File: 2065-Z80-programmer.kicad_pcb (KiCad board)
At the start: 2 copper layers, 100 x 65 mm, 29 parts, among them J1 Conn_01x05, J2 Conn_02x20_Counter_Clockwise, J3 Conn_01x02, J4 Conn_02x20_Odd_Even, Q1 2N7000, Q2 2N7000, Q3 PN2222, U1 MCP23017-E_SP, U2 MCP23017-E_SP

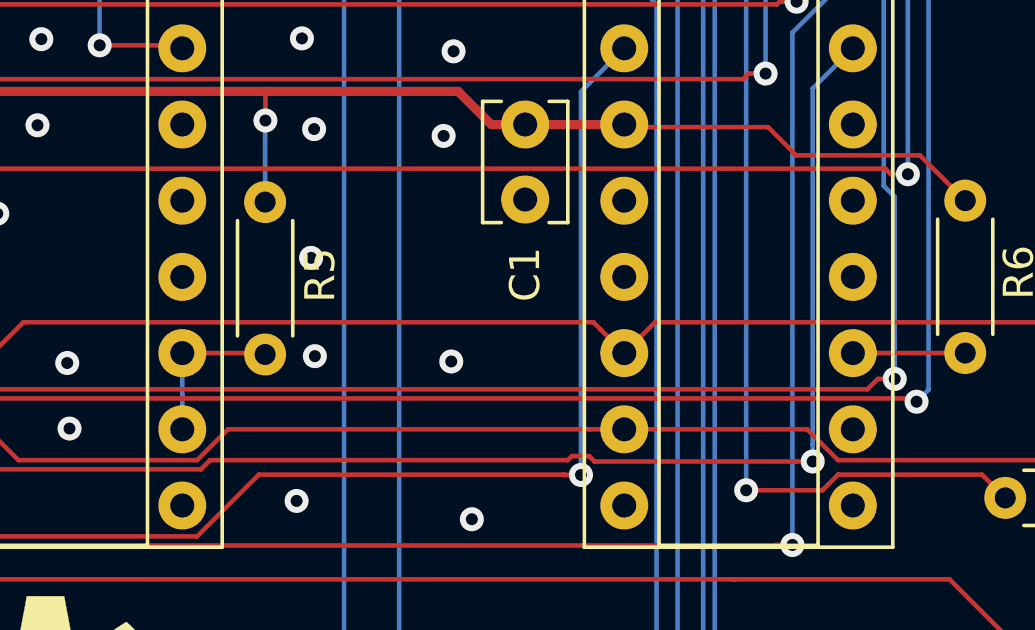
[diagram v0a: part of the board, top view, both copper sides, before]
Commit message: Pull up /RESET
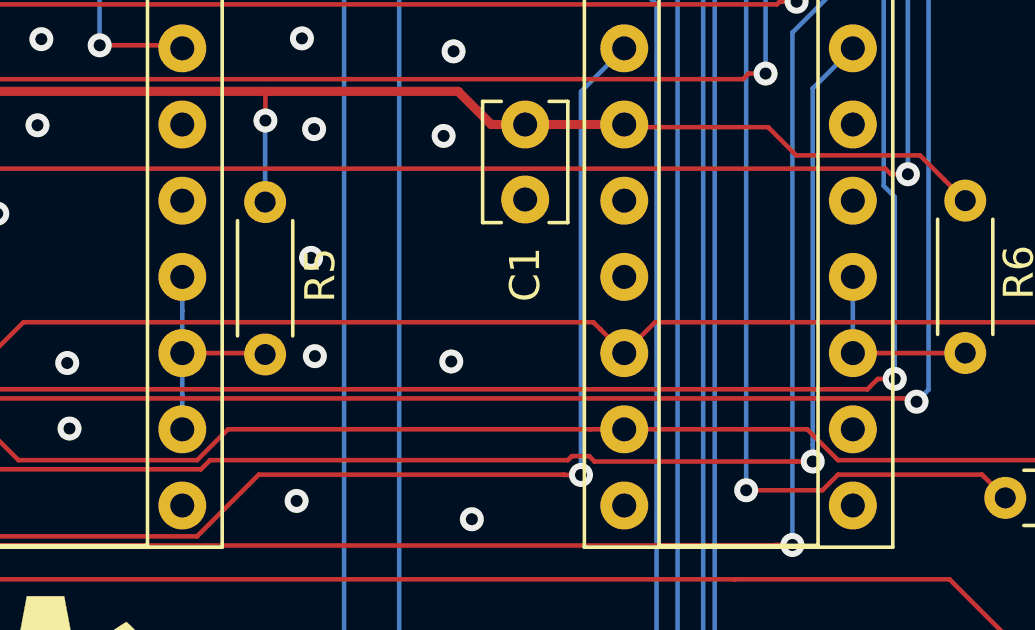
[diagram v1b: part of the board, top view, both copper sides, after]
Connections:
- U1 pad 18: Net-(U1-Pad18) -> Net-(R5-Pad1)
- U2 pad 18: Net-(U2-Pad18) -> Net-(R6-Pad1)
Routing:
- net Net-(R5-Pad1): track 5.32 -> 7.86 mm
- net Net-(R6-Pad1): track 3.75 -> 6.29 mm

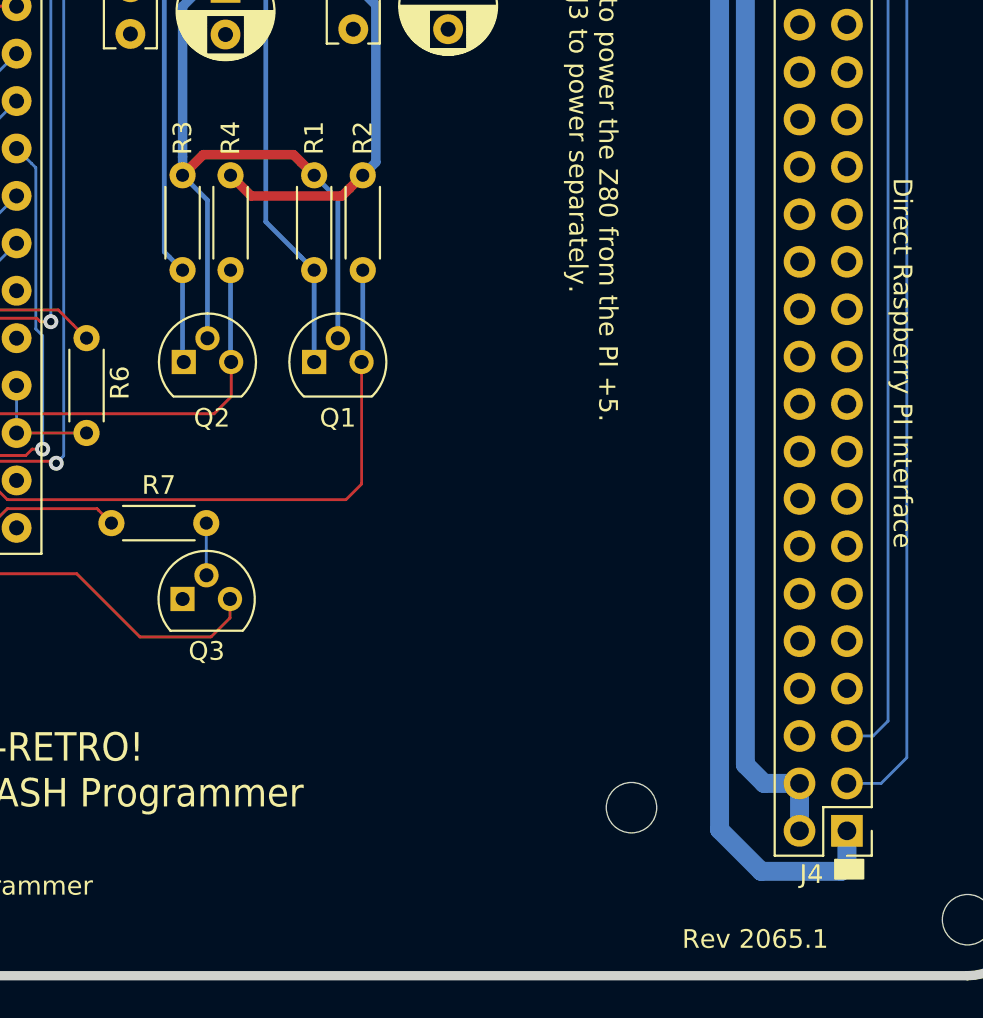
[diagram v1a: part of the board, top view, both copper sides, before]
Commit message: Add 5V clamping diodes to I2C lines Move mounting hole clear of user-1 header
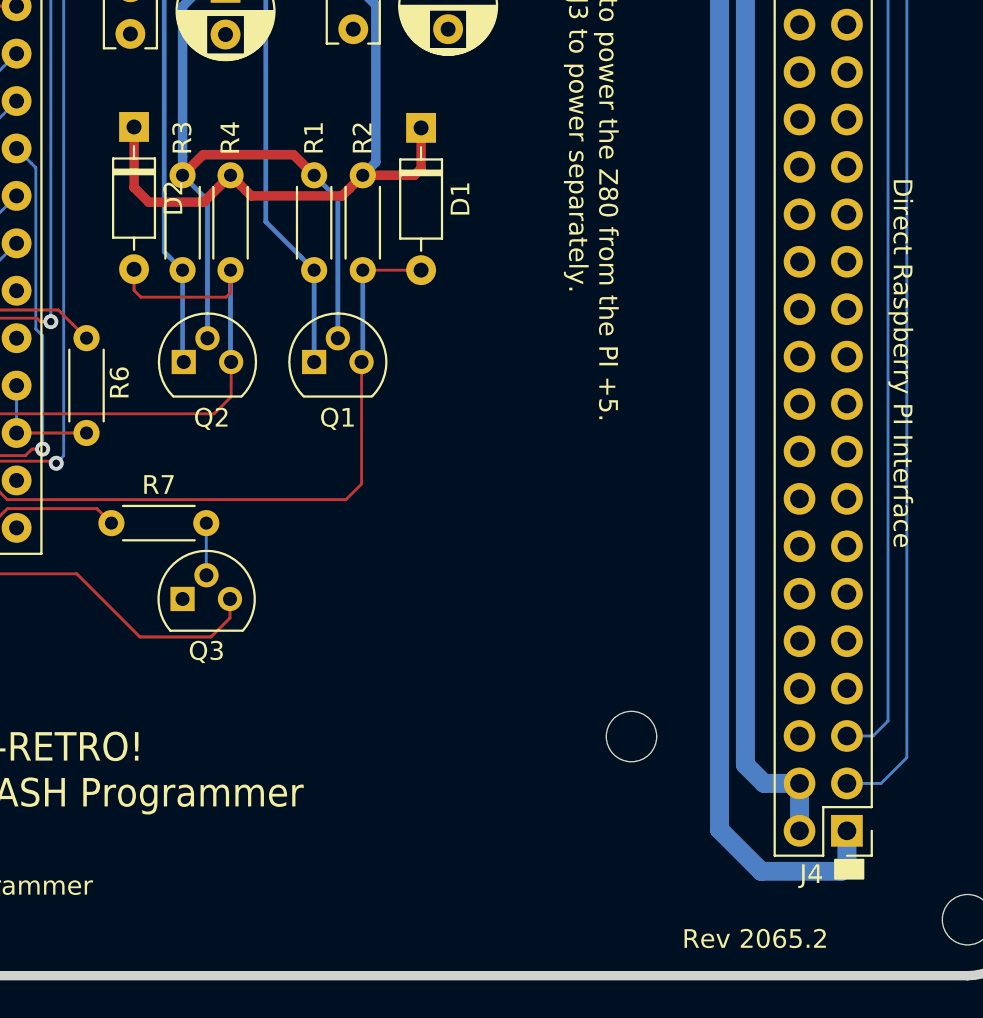
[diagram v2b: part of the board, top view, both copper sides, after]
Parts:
- added D1: 1N914, Diode_THT:D_DO-35_SOD27_P7.62mm_Horizontal, F.Cu at (152.7, 74.6)
- added D2: 1N914, Diode_THT:D_DO-35_SOD27_P7.62mm_Horizontal, F.Cu at (137.4, 74.5)
- moved H5 3.81 mm to (164.0, 107.2)
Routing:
- net +5V: track 179.0 -> 193.7 mm
- net /SCK: track 49.9 -> 57.7 mm
- net /SDA: track 61.6 -> 64.7 mm
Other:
- board text added: "Rev 2065.2"
- board text removed: "Rev 2065.1"
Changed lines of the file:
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@@
     (thickness 1.6)
     (drawings 29)
-    (tracks 476)
+    (tracks 490)
     (zones 0)
-    (modules 29)
+    (modules 31)
     (nets 86)
   )
   (page A4)
+  (title_block
+    (date 2021-10-18)
+    (rev 2.0)
+  )
   (layers
     (0 F.Cu signal)
@@
     (add_net "Net-(U2-Pad20)")
   )
+  (module Diode_THT:D_DO-35_SOD27_P7.62mm_Horizontal (layer F.Cu)
+    (at 137.35558 74.53884 270)
+    (descr "Diode, DO-35_SOD27 series, Axial, Horizontal, pin pitch=7.62mm, , length*diameter=4*2mm^2, , http://www.diodes.com/_files/packages/DO-35.pdf")
+    (tags "Diode DO-35_SOD27 series Axial Horizontal pin pitch 7.62mm  length 4mm diameter 2mm")
+    (fp_text reference D2 (at 3.81 -2.12 90) (layer F.SilkS)
+      (effects (font (size 1 1) (thickness 0.15)))
+    )
+    (fp_text value 1N914 (at 3.81 2.12 90) (layer F.Fab)
+      (effects (font (size 1 1) (thickness 0.15)))
+    )
+    (fp_text user K (at 0 -1.8 90) (layer F.SilkS) hide
+      (effects (font (size 1 1) (thickness 0.15)))
+    )
+    (fp_text user K (at 0 -1.8 90) (layer F.Fab)
+      (effects (font (size 1 1) (thickness 0.15)))
+    )
+    (fp_text user %R (at 4.11 0 90) (layer F.Fab)
+      (effects (font (size 0.8 0.8) (thickness 0.12)))
+    )
+    (fp_line (start 8.67 -1.25) (end -1.05 -1.25) (layer F.CrtYd) (width 0.05))
+    (fp_line (start 8.67 1.25) (end 8.67 -1.25) (layer F.CrtYd) (width 0.05))
+    (fp_line (start -1.05 1.25) (end 8.67 1.25) (layer F.CrtYd) (width 0.05))
+    (fp_line (start -1.05 -1.25) (end -1.05 1.25) (layer F.CrtYd) (width 0.05))
+    (fp_line (start 2.29 -1.12) (end 2.29 1.12) (layer F.SilkS) (width 0.12))
+    (fp_line (start 2.53 -1.12) (end 2.53 1.12) (layer F.SilkS) (width 0.12))
+    (fp_line (start 2.41 -1.12) (end 2.41 1.12) (layer F.SilkS) (width 0.12))
+    (fp_line (start 6.58 0) (end 5.93 0) (layer F.SilkS) (width 0.12))
+    (fp_line (start 1.04 0) (end 1.69 0) (layer F.SilkS) (width 0.12))
+    (fp_line (start 5.93 -1.12) (end 1.69 -1.12) (layer F.SilkS) (width 0.12))
+    (fp_line (start 5.93 1.12) (end 5.93 -1.12) (layer F.SilkS) (width 0.12))
+    (fp_line (start 1.69 1.12) (end 5.93 1.12) (layer F.SilkS) (width 0.12))
+    (fp_line (start 1.69 -1.12) (end 1.69 1.12) (layer F.SilkS) (width 0.12))
+    (fp_line (start 2.31 -1) (end 2.31 1) (layer F.Fab) (width 0.1))
+    (fp_line (start 2.51 -1) (end 2.51 1) (layer F.Fab) (width 0.1))
+    (fp_line (start 2.41 -1) (end 2.41 1) (layer F.Fab) (width 0.1))
+    (fp_line (start 7.62 0) (end 5.81 0) (layer F.Fab) (width 0.1))
+    (fp_line (start 0 0) (end 1.81 0) (layer F.Fab) (width 0.1))
+    (fp_line (start 5.81 -1) (end 1.81 -1) (layer F.Fab) (width 0.1))
+    (fp_line (start 5.81 1) (end 5.81 -1) (layer F.Fab) (width 0.1))
+    (fp_line (start 1.81 1) (end 5.81 1) (layer F.Fab) (width 0.1))
+    (fp_line (start 1.81 -1) (end 1.81 1) (layer F.Fab) (width 0.1))
+    (pad 2 thru_hole oval (at 7.62 0 270) (size 1.6 1.6) (drill 0.8) (layers *.Cu *.Mask)
+      (net 13 /SCK))
+    (pad 1 thru_hole rect (at 0 0 270) (size 1.6 1.6) (drill 0.8) (layers *.Cu *.Mask)
+      (net 12 +5V))
+    (model ${KISYS3DMOD}/Diode_THT.3dshapes/D_DO-35_SOD27_P7.62mm_Horizontal.wrl
+      (at (xyz 0 0 0))
+      (scale (xyz 1 1 1))
+      (rotate (xyz 0 0 0))
+    )
+  )
+  (module Diode_THT:D_DO-35_SOD27_P7.62mm_Horizontal (layer F.Cu)
+    (at 152.7302 74.58964 270)
+    (descr "Diode, DO-35_SOD27 series, Axial, Horizontal, pin pitch=7.62mm, , length*diameter=4*2mm^2, , http://www.diodes.com/_files/packages/DO-35.pdf")
+    (tags "Diode DO-35_SOD27 series Axial Horizontal pin pitch 7.62mm  length 4mm diameter 2mm")
+    (fp_text reference D1 (at 3.81 -2.12 90) (layer F.SilkS)
+      (effects (font (size 1 1) (thickness 0.15)))
+    )
+    (fp_text value 1N914 (at 3.81 2.12 90) (layer F.Fab)
+      (effects (font (size 1 1) (thickness 0.15)))
+    )
+    (fp_text user K (at 0 -1.8 90) (layer F.SilkS) hide
+      (effects (font (size 1 1) (thickness 0.15)))
+    )
+    (fp_text user K (at 0 -1.8 90) (layer F.Fab)
+      (effects (font (size 1 1) (thickness 0.15)))
+    )
+    (fp_text user %R (at 4.11 0 90) (layer F.Fab)
+      (effects (font (size 0.8 0.8) (thickness 0.12)))
+    )
+    (fp_line (start 8.67 -1.25) (end -1.05 -1.25) (layer F.CrtYd) (width 0.05))
+    (fp_line (start 8.67 1.25) (end 8.67 -1.25) (layer F.CrtYd) (width 0.05))
+    (fp_line (start -1.05 1.25) (end 8.67 1.25) (layer F.CrtYd) (width 0.05))
+    (fp_line (start -1.05 -1.25) (end -1.05 1.25) (layer F.CrtYd) (width 0.05))
+    (fp_line (start 2.29 -1.12) (end 2.29 1.12) (layer F.SilkS) (width 0.12))
+    (fp_line (start 2.53 -1.12) (end 2.53 1.12) (layer F.SilkS) (width 0.12))
+    (fp_line (start 2.41 -1.12) (end 2.41 1.12) (layer F.SilkS) (width 0.12))
+    (fp_line (start 6.58 0) (end 5.93 0) (layer F.SilkS) (width 0.12))
+    (fp_line (start 1.04 0) (end 1.69 0) (layer F.SilkS) (width 0.12))
+    (fp_line (start 5.93 -1.12) (end 1.69 -1.12) (layer F.SilkS) (width 0.12))
+    (fp_line (start 5.93 1.12) (end 5.93 -1.12) (layer F.SilkS) (width 0.12))
+    (fp_line (start 1.69 1.12) (end 5.93 1.12) (layer F.SilkS) (width 0.12))
+    (fp_line (start 1.69 -1.12) (end 1.69 1.12) (layer F.SilkS) (width 0.12))
+    (fp_line (start 2.31 -1) (end 2.31 1) (layer F.Fab) (width 0.1))
+    (fp_line (start 2.51 -1) (end 2.51 1) (layer F.Fab) (width 0.1))
+    (fp_line (start 2.41 -1) (end 2.41 1) (layer F.Fab) (width 0.1))
+    (fp_line (start 7.62 0) (end 5.81 0) (layer F.Fab) (width 0.1))
+    (fp_line (start 0 0) (end 1.81 0) (layer F.Fab) (width 0.1))
+    (fp_line (start 5.81 -1) (end 1.81 -1) (layer F.Fab) (width 0.1))
+    (fp_line (start 5.81 1) (end 5.81 -1) (layer F.Fab) (width 0.1))
+    (fp_line (start 1.81 1) (end 5.81 1) (layer F.Fab) (width 0.1))
+    (fp_line (start 1.81 -1) (end 1.81 1) (layer F.Fab) (width 0.1))
+    (pad 2 thru_hole oval (at 7.62 0 270) (size 1.6 1.6) (drill 0.8) (layers *.Cu *.Mask)
+      (net 11 /SDA))
+    (pad 1 thru_hole rect (at 0 0 270) (size 1.6 1.6) (drill 0.8) (layers *.Cu *.Mask)
+      (net 12 +5V))
+    (model ${KISYS3DMOD}/Diode_THT.3dshapes/D_DO-35_SOD27_P7.62mm_Horizontal.wrl
+      (at (xyz 0 0 0))
+      (scale (xyz 1 1 1))
+      (rotate (xyz 0 0 0))
+    )
+  )
   (module MountingHole:MountingHole_2.7mm_M2.5_DIN965 (layer F.Cu)
-    (at 164 111)
+    (at 164 107.19)
     (descr "Mounting Hole 2.7mm, no annular, M2.5, DIN965")
     (tags "mounting hole 2.7mm no annular m2.5 din965")
@@
     )
   )
-  (gr_text "Rev 2065.1" (at 166.70528 118.04396) (layer F.SilkS)
+  (gr_text "Rev 2065.2" (at 166.70528 118.04396) (layer F.SilkS)
     (effects (font (size 1 1) (thickness 0.15)) (justify left))
   )
@@
   (segment (start 149.542 93.663) (end 149.542 87.128) (width 0.1524) (layer F.Cu) (net 11))
   (segment (start 148.704399 94.500601) (end 149.542 93.663) (width 0.1524) (layer F.Cu) (net 11))
+  (segment (start 152.72856 82.208) (end 152.7302 82.20964) (width 0.1524) (layer F.Cu) (net 11))
+  (segment (start 149.606 82.208) (end 152.72856 82.208) (width 0.1524) (layer F.Cu) (net 11))
   (segment (start 155.512 58.166) (end 148.082 58.166) (width 1.016) (layer B.Cu) (net 12))
   (segment (start 148.082 65.786) (end 149.098 66.802) (width 0.508) (layer B.Cu) (net 12))
@@
   (segment (start 96.65863 83.312) (end 96.00202 83.96861) (width 0.3048) (layer F.Cu) (net 12))
   (segment (start 92.46842 83.96861) (end 91.75 83.96861) (width 0.3048) (layer F.Cu) (net 12))
+  (segment (start 149.606 77.128) (end 152.361 77.128) (width 0.508) (layer F.Cu) (net 12))
+  (segment (start 152.7302 76.7588) (end 152.7302 74.58964) (width 0.508) (layer F.Cu) (net 12))
+  (segment (start 152.361 77.128) (end 152.7302 76.7588) (width 0.508) (layer F.Cu) (net 12))
+  (segment (start 142.524 77.128) (end 141.08726 78.56474) (width 0.508) (layer F.Cu) (net 12))
+  (segment (start 141.08726 78.56474) (end 138.14044 78.56474) (width 0.508) (layer F.Cu) (net 12))
+  (segment (start 137.35558 77.77988) (end 137.35558 74.53884) (width 0.508) (layer F.Cu) (net 12))
+  (segment (start 138.14044 78.56474) (end 137.35558 77.77988) (width 0.508) (layer F.Cu) (net 12))
   (segment (start 142.524 87.0942) (end 142.5578 87.128) (width 0.254) (layer B.Cu) (net 13))
   (segment (start 142.524 82.208) (end 142.524 87.0942) (width 0.254) (layer B.Cu) (net 13))
@@
   (segment (start 102.3874 90.932) (end 103.416001 89.903399) (width 0.1524) (layer F.Cu) (net 13))
   (segment (start 101.092 90.932) (end 102.3874 90.932) (width 0.1524) (layer F.Cu) (net 13))
+  (segment (start 137.35558 83.29021) (end 137.72027 83.6549) (width 0.1524) (layer F.Cu) (net 13))
+  (segment (start 137.35558 82.15884) (end 137.35558 83.29021) (width 0.1524) (layer F.Cu) (net 13))
+  (segment (start 137.72027 83.6549) (end 142.29334 83.6549) (width 0.1524) (layer F.Cu) (net 13))
+  (segment (start 142.524 83.42424) (end 142.524 82.208) (width 0.1524) (layer F.Cu) (net 13))
+  (segment (start 142.29334 83.6549) (end 142.524 83.42424) (width 0.1524) (layer F.Cu) (net 13))
   (via (at 110.220661 71.640601) (size 0.8) (drill 0.4) (layers F.Cu B.Cu) (net 14))
   (segment (start 110.220661 64.500661) (end 108.712 62.992) (width 0.1524) (layer B.Cu) (net 14))

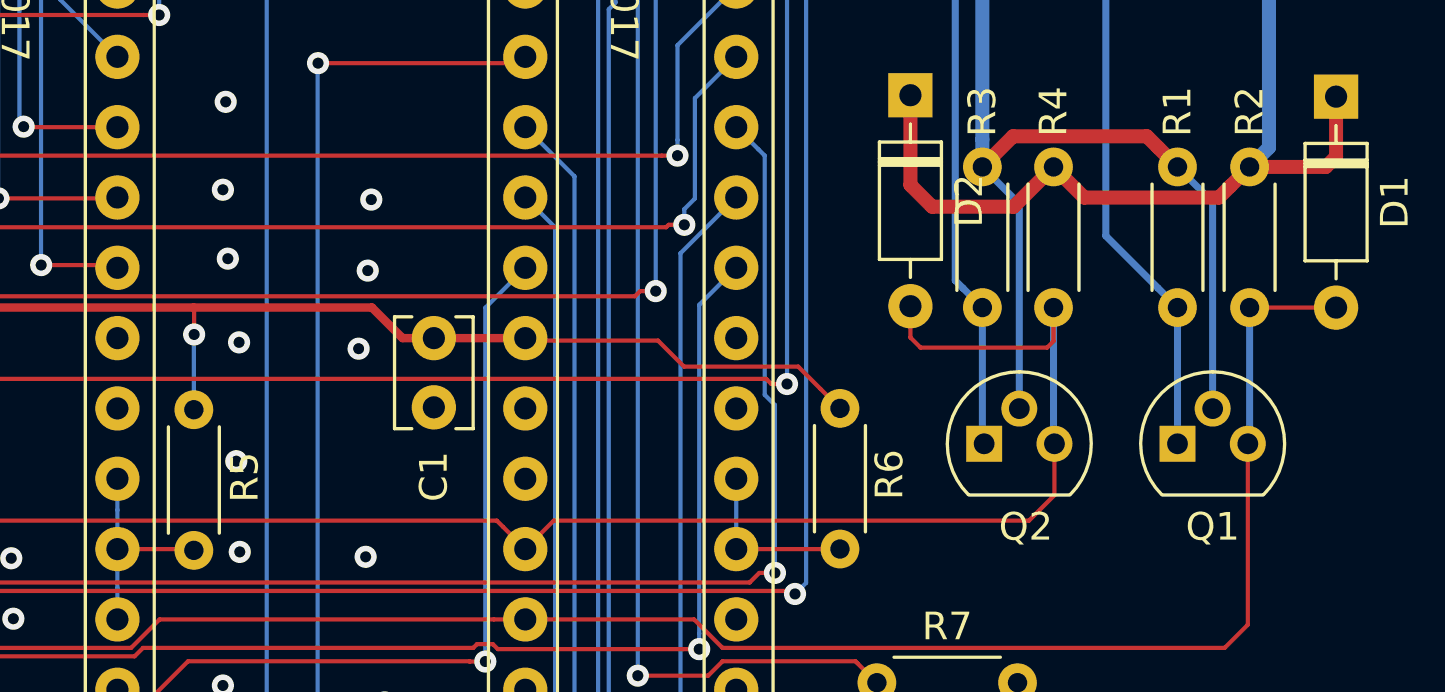
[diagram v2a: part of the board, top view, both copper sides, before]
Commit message: Cosmetic silkscreen cleanup
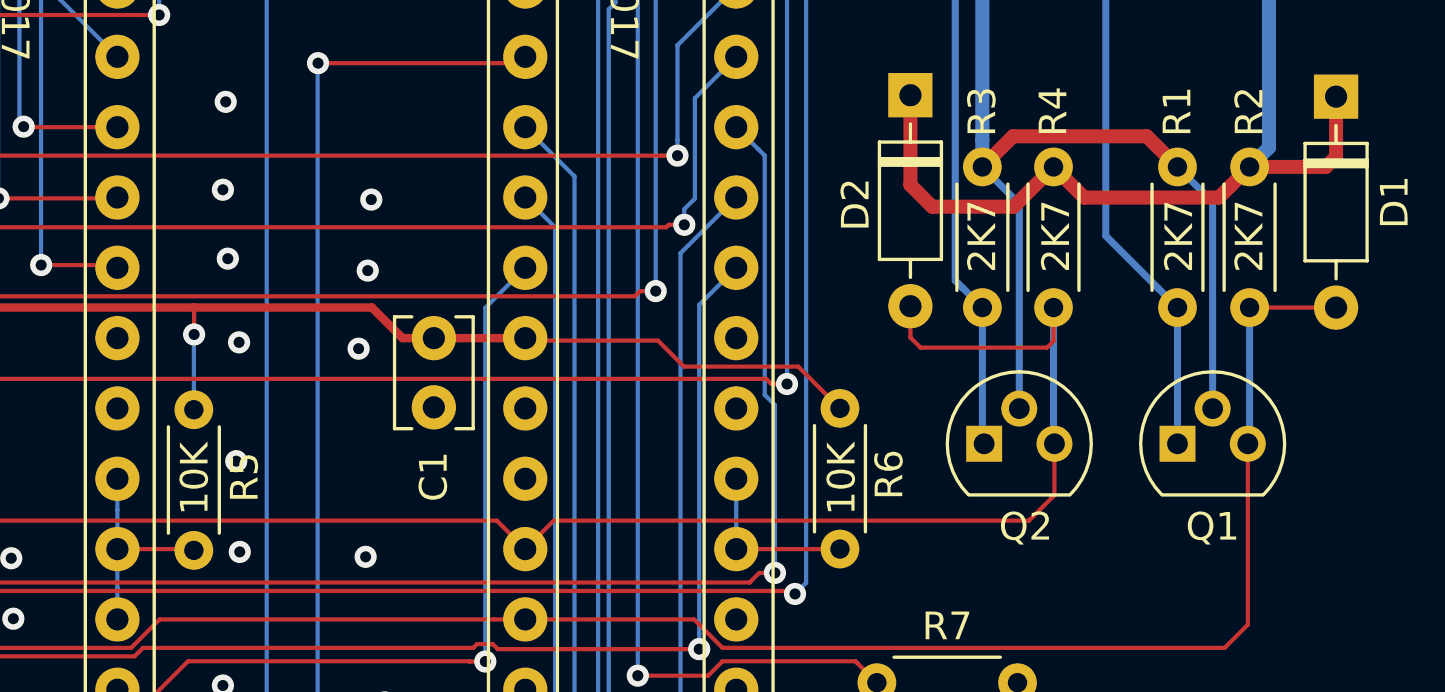
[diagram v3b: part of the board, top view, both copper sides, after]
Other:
- board text added: "10K"
- board text added: "2K7"
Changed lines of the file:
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@@
   (general
     (thickness 1.6)
-    (drawings 29)
+    (drawings 35)
     (tracks 490)
     (zones 0)
@@
     (descr "Diode, DO-35_SOD27 series, Axial, Horizontal, pin pitch=7.62mm, , length*diameter=4*2mm^2, , http://www.diodes.com/_files/packages/DO-35.pdf")
     (tags "Diode DO-35_SOD27 series Axial Horizontal pin pitch 7.62mm  length 4mm diameter 2mm")
-    (fp_text reference D2 (at 3.81 -2.12 90) (layer F.SilkS)
+    (fp_text reference D2 (at 3.94716 1.97358 90) (layer F.SilkS)
       (effects (font (size 1 1) (thickness 0.15)))
     )
@@
     )
   )
+  (gr_text 10K (at 111.506 88.392 90) (layer F.SilkS)
+    (effects (font (size 1 1) (thickness 0.15)))
+  )
+  (gr_text 10K (at 134.874 88.392 90) (layer F.SilkS)
+    (effects (font (size 1 1) (thickness 0.15)))
+  )
+  (gr_text 2K7 (at 149.606 79.629 90) (layer F.SilkS)
+    (effects (font (size 1 1) (thickness 0.15)))
+  )
+  (gr_text 2K7 (at 147.066 79.629 90) (layer F.SilkS)
+    (effects (font (size 1 1) (thickness 0.15)))
+  )
+  (gr_text 2K7 (at 142.621 79.629 90) (layer F.SilkS)
+    (effects (font (size 1 1) (thickness 0.15)))
+  )
+  (gr_text 2K7 (at 139.954 79.629 90) (layer F.SilkS)
+    (effects (font (size 1 1) (thickness 0.15)))
+  )
   (gr_text "Rev 2065.2" (at 166.70528 118.04396) (layer F.SilkS)
